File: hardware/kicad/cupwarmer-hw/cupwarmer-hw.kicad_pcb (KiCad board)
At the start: 4 copper layers, 56 x 56 mm, 50 parts, among them J1 I2C Service, Q1 AO3400 SOT-23, U1 STWLC38JRM

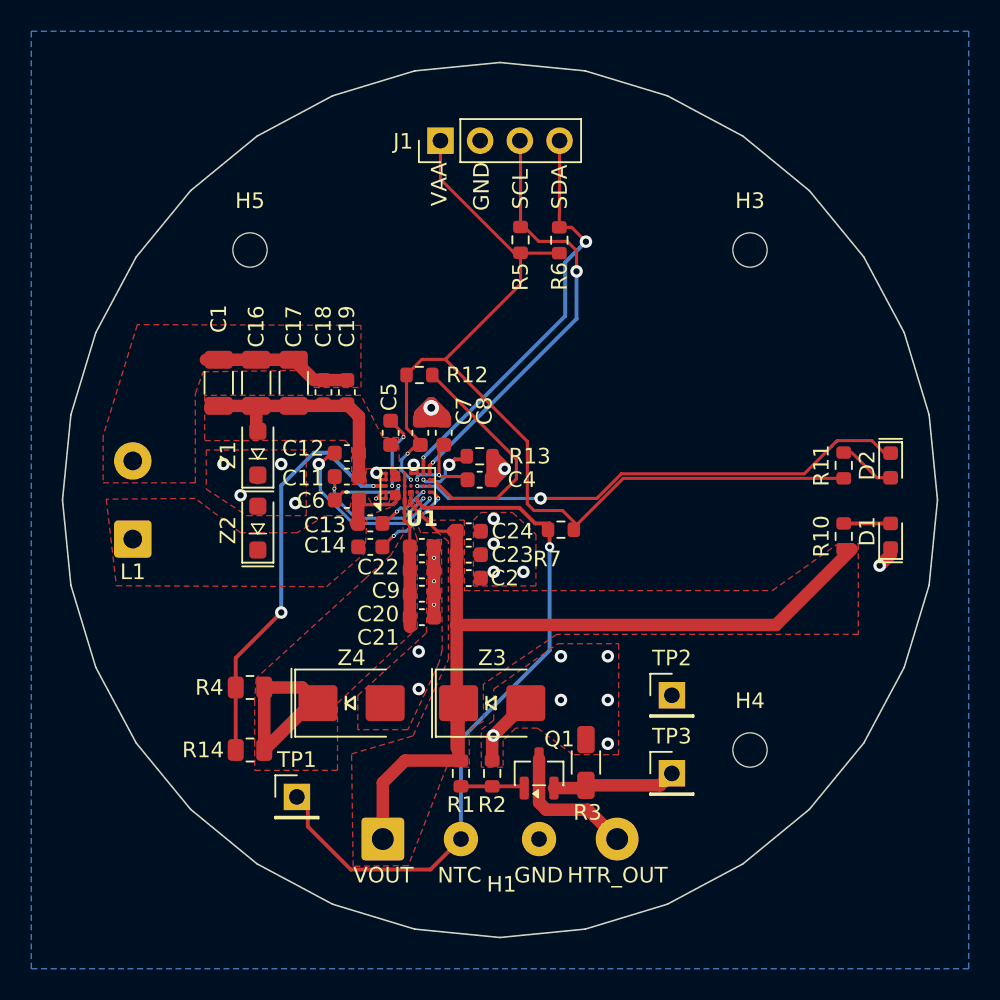
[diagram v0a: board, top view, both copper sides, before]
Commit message: Update PCB layout state
add C25
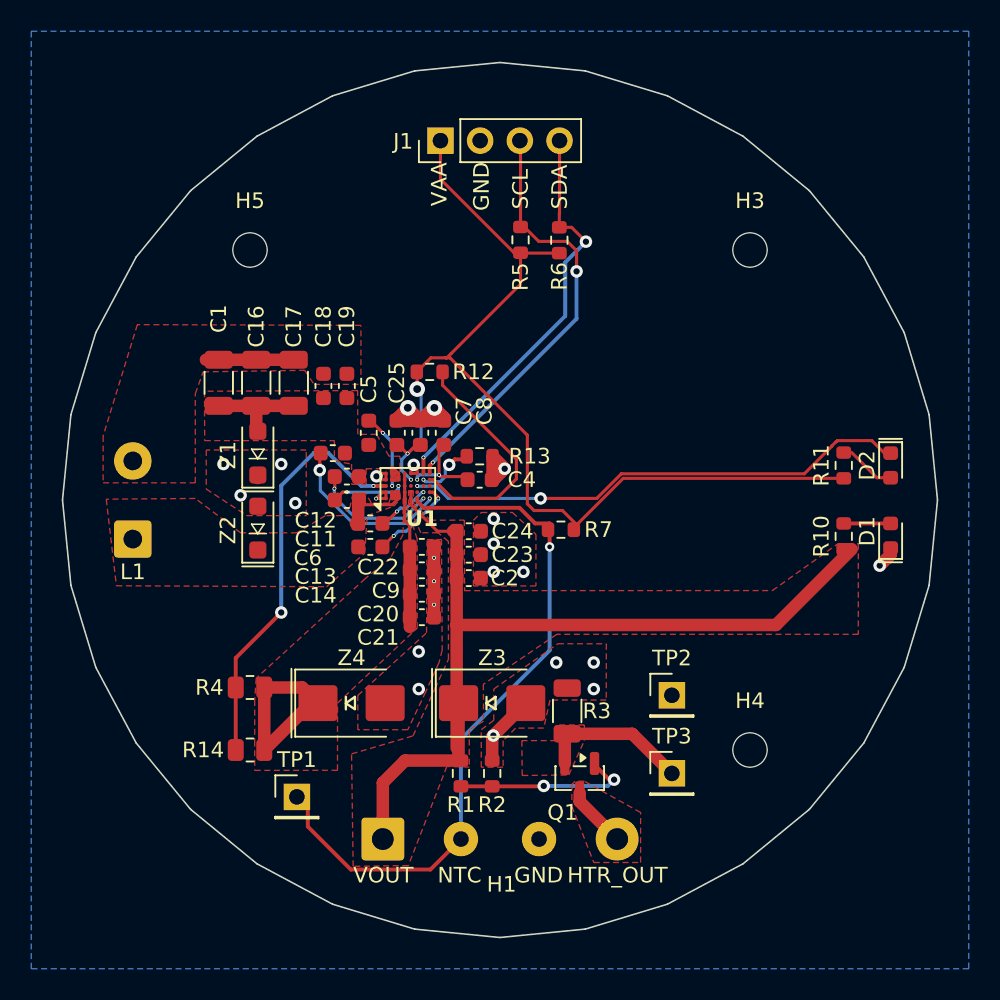
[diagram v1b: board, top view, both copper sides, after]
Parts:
- added C25: 100nF, Capacitor_SMD:C_0603_1608Metric, F.Cu at (93.4, 95.7)
- moved R3 3.51 mm to (104.3, 113.5)
- moved Q1 2.62 mm to (105.1, 117.8), turned to -90 degrees
- moved C5 1.40 mm to (91.6, 95.7)
- moved C12 0.90 mm to (89.3, 97.0)
- moved R12 0.69 mm to (95.5, 91.8)
- moved C18 0.40 mm to (88.7, 92.7)
- moved C19 0.40 mm to (90.2, 92.7)
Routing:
- net /rx-power/AC1: track 18.2 -> 9.80 mm
- net Net-(Q1-G): track 4.10 -> 11.7 mm, vias 0 -> 2
- net /heater-control/HEATER_OUT: track 8.77 -> 3.96 mm
- net /rx-power/AC1 COIL: track 9.76 -> 5.83 mm
- net SYS_GND: track 26.4 -> 29.6 mm, vias 25 -> 24
- net RX_VAA: track 65.1 -> 66.8 mm, vias 2 -> 3
- net I_HEATER_MON: track 8.12 -> 9.71 mm
- added copper zone on F.Cu, net /heater-control/HEATER_OUT
- added copper zone on F.Cu, net I_HEATER_MON
